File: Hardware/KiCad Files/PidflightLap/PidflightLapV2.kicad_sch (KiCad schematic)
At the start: 27 parts, among them SW1 SW_SPST, U1 HC_06, U2 RX5808, U3 Arduino_Nano_v3.x, U4 RX5808, U5 Arduino_Nano_v3.x, U6 RX5808, U7 Arduino_Nano_v3.x, U8 RX5808, U9 Arduino_Nano_v3.x

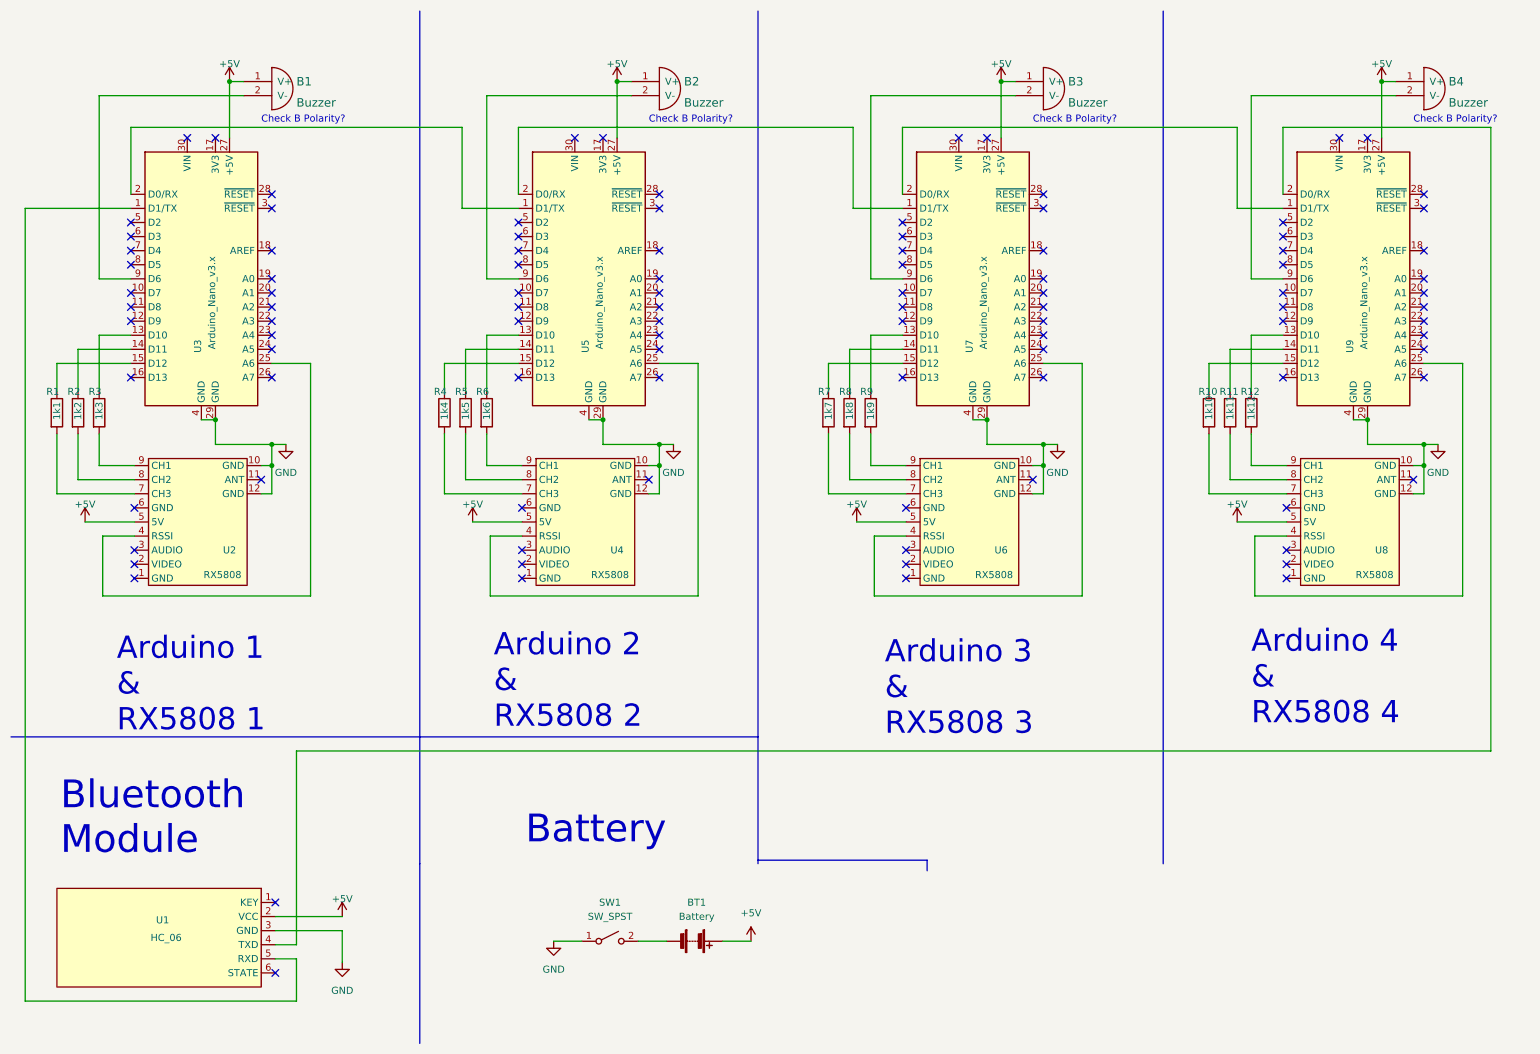
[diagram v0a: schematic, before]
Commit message: Cleaned Up Files and added Bevels and BOM
removed some pointless KiCAD files I had accidently added created as well as beveled all the 90 degree connections on the PCB file
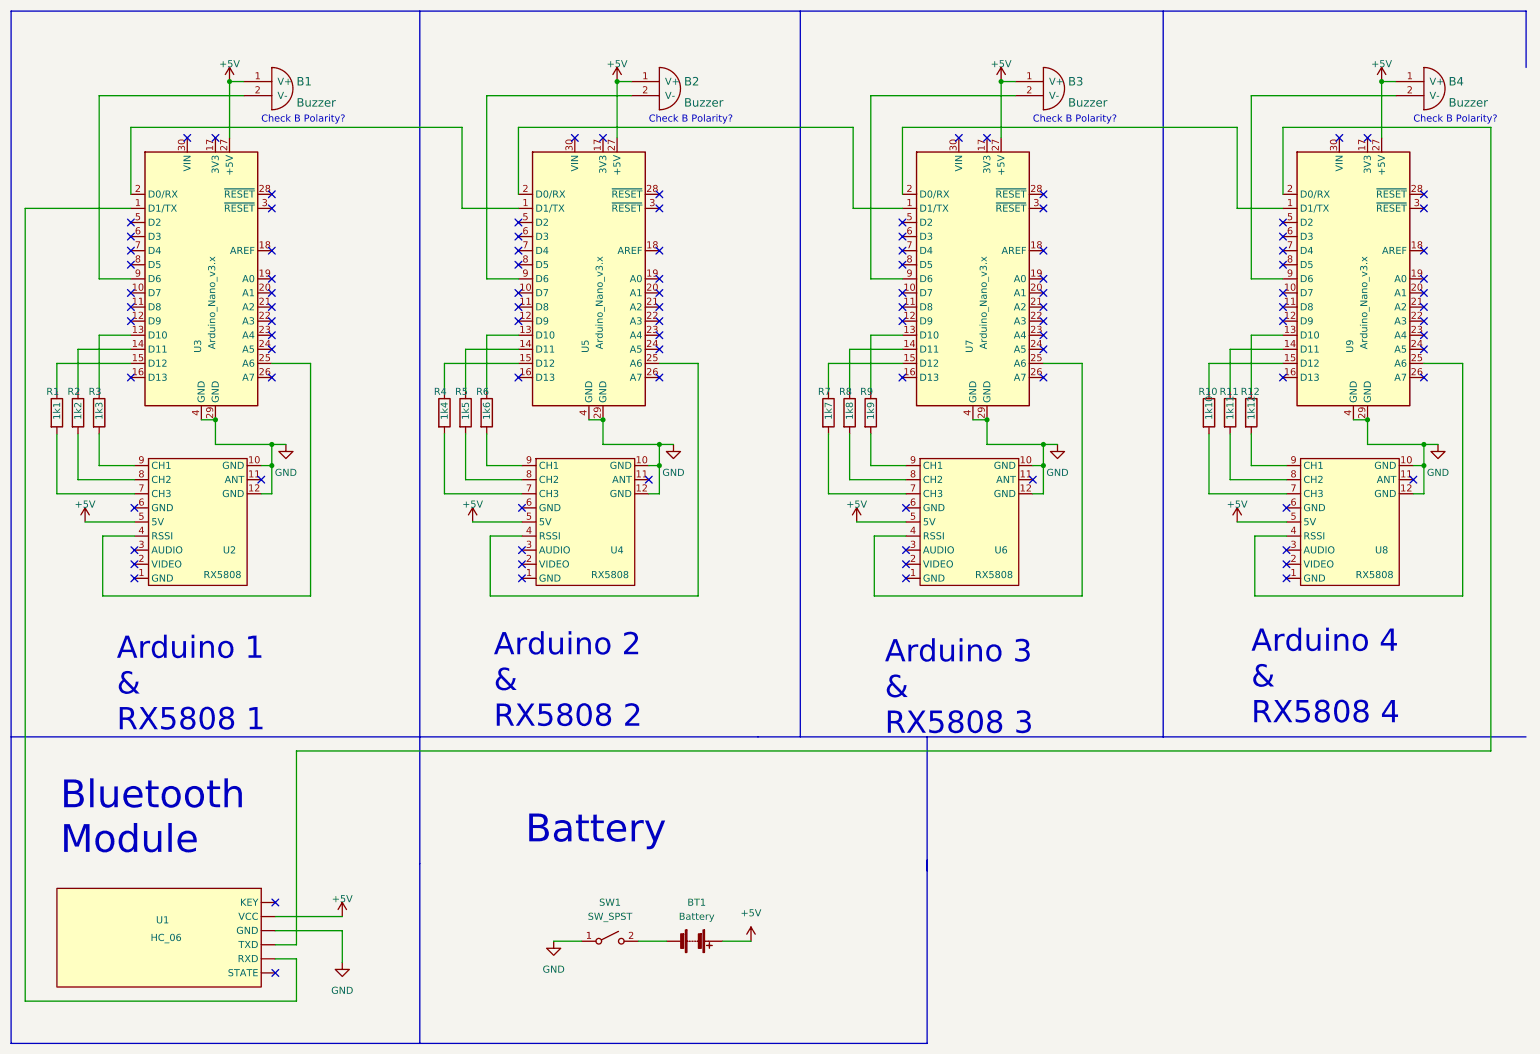
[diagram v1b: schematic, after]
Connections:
- net +5V: now also U1. (VCC); no longer U1.2 (VCC)
- net GND: now also U1. (VCC); no longer U1.3 (GND)
- net at U9.2 (D0/RX): now also U1. (VCC); no longer U1.4 (TXD)
- net at U3.1 (D1/TX): now also U1. (VCC); no longer U1.5 (RXD)
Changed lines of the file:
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@@
   (junction (at 187.96 85.725) (diameter 0) (color 0 0 0 1)
   )
+  (junction (at 128.905 90.17) (diameter 0) (color 0 0 0 1)
+  )
+  (junction (at 121.285 24.765) (diameter 0) (color 255 0 0 1)
+  )
   (junction (at 48.895 85.725) (diameter 0) (color 0 0 0 1)
-  )
-  (junction (at 128.905 90.17) (diameter 0) (color 0 0 0 1)
-  )
-  (junction (at 121.285 24.765) (diameter 0) (color 255 0 0 1)
   )
   (no_connect (at 118.745 34.925))
@@
     (stroke (width 0) (type default) (color 0 0 0 1))
   )
+  (polyline (pts (xy 12.065 12.065) (xy 285.115 12.065))
+    (stroke (width 0) (type default) (color 0 0 0 0))
+  )
   (wire (pts (xy 33.655 45.085) (xy 33.655 33.02))
     (stroke (width 0) (type default) (color 255 0 255 1))
@@
     (stroke (width 0) (type default) (color 0 0 0 1))
   )
+  (wire (pts (xy 48.895 85.725) (xy 48.895 90.17))
+    (stroke (width 0) (type default) (color 0 0 0 1))
+  )
   (wire (pts (xy 27.94 88.265) (xy 27.94 93.98))
     (stroke (width 0) (type default) (color 246 255 28 1))
@@
     (stroke (width 0) (type default) (color 0 0 0 1))
   )
+  (polyline (pts (xy 12.065 12.065) (xy 12.065 198.12))
+    (stroke (width 0) (type default) (color 0 0 0 0))
+  )
   (wire (pts (xy 63.5 190.5) (xy 63.5 182.88))
     (stroke (width 0) (type default) (color 255 0 255 1))
@@
   )
   (wire (pts (xy 59.055 99.06) (xy 57.15 99.06))
-    (stroke (width 0) (type default) (color 0 0 0 1))
-  )
-  (wire (pts (xy 48.895 85.725) (xy 48.895 90.17))
     (stroke (width 0) (type default) (color 0 0 0 1))
   )
@@
     (stroke (width 0) (type default) (color 0 0 0 1))
   )
+  (polyline (pts (xy 154.305 12.065) (xy 154.305 142.875))
+    (stroke (width 0) (type default) (color 0 0 0 0))
+  )
   (wire (pts (xy 187.96 85.725) (xy 187.96 90.17))
     (stroke (width 0) (type default) (color 0 0 0 1))
@@
     (stroke (width 0) (type default) (color 246 255 28 1))
   )
+  (polyline (pts (xy 285.115 12.065) (xy 285.115 22.225))
+    (stroke (width 0) (type default) (color 0 0 0 0))
+  )
   (wire (pts (xy 256.54 90.17) (xy 266.7 90.17))
     (stroke (width 0) (type default) (color 0 0 0 1))
@@
     (stroke (width 0) (type default) (color 0 0 0 1))
   )
+  (polyline (pts (xy 85.725 198.12) (xy 177.165 198.12))
+    (stroke (width 0) (type default) (color 0 0 0 0))
+  )
   (wire (pts (xy 93.345 33.02) (xy 93.345 47.625))
     (stroke (width 0) (type default) (color 255 0 255 1))
@@
   (wire (pts (xy 27.94 80.645) (xy 27.94 70.485))
     (stroke (width 0) (type default) (color 246 255 28 1))
+  )
+  (polyline (pts (xy 146.685 142.875) (xy 219.71 142.875))
+    (stroke (width 0) (type default) (color 0 0 0 0))
   )
   (wire (pts (xy 190.5 24.765) (xy 193.04 24.765))
@@
     (stroke (width 0) (type default) (color 0 0 0 1))
   )
-  (polyline (pts (xy 219.71 12.065) (xy 219.71 165.735))
+  (polyline (pts (xy 219.71 12.065) (xy 219.71 142.875))
     (stroke (width 0) (type default) (color 0 0 0 0))
   )
@@
     (stroke (width 0) (type default) (color 255 0 255 1))
   )
+  (polyline (pts (xy 219.71 142.875) (xy 285.115 142.875))
+    (stroke (width 0) (type default) (color 0 0 0 0))
+  )
   (polyline (pts (xy 85.725 12.065) (xy 85.725 165.735))
     (stroke (width 0) (type default) (color 0 0 0 0))
@@
     (stroke (width 0) (type default) (color 0 0 0 1))
   )
+  (wire (pts (xy 34.29 106.68) (xy 28.575 106.68))
+    (stroke (width 0) (type default) (color 0 0 0 0))
+  )
+  (wire (pts (xy 167.64 106.68) (xy 167.64 117.475))
+    (stroke (width 0) (type default) (color 0 0 0 0))
+  )
   (wire (pts (xy 46.355 85.725) (xy 48.895 85.725))
     (stroke (width 0) (type default) (color 0 0 0 1))
-  )
-  (wire (pts (xy 34.29 106.68) (xy 28.575 106.68))
-    (stroke (width 0) (type default) (color 0 0 0 0))
-  )
-  (wire (pts (xy 167.64 106.68) (xy 167.64 117.475))
-    (stroke (width 0) (type default) (color 0 0 0 0))
   )
   (wire (pts (xy 235.585 27.305) (xy 261.62 27.305))
@@
     (stroke (width 0) (type default) (color 255 0 0 1))
   )
-  (polyline (pts (xy 146.685 165.1) (xy 177.165 165.1))
-    (stroke (width 0) (type default) (color 0 0 0 0))
-  )
   (wire (pts (xy 104.14 96.52) (xy 93.98 96.52))
     (stroke (width 0) (type default) (color 15 255 0 1))
@@
     (stroke (width 0) (type default) (color 0 0 0 0))
   )
-  (polyline (pts (xy 146.685 12.065) (xy 146.685 165.735))
-    (stroke (width 0) (type default) (color 0 0 0 0))
-  )
   (wire (pts (xy 266.7 93.98) (xy 266.7 99.06))
     (stroke (width 0) (type default) (color 0 0 0 1))
@@
   (wire (pts (xy 128.905 90.17) (xy 131.445 90.17))
     (stroke (width 0) (type default) (color 0 0 0 1))
+  )
+  (polyline (pts (xy 177.165 198.12) (xy 177.165 142.875))
+    (stroke (width 0) (type default) (color 0 0 0 0))
   )
   (wire (pts (xy 167.005 70.485) (xy 172.72 70.485))
@@
   (wire (pts (xy 235.585 88.265) (xy 235.585 93.98))
     (stroke (width 0) (type default) (color 246 255 28 1))
+  )
+  (polyline (pts (xy 85.725 198.12) (xy 12.065 198.12))
+    (stroke (width 0) (type default) (color 0 0 0 0))
   )
   (wire (pts (xy 34.29 99.06) (xy 20.32 99.06))
@@
       (effects (font (size 1.27 1.27)) hide)
     )
-    (pin "1")
-    (pin "2")
-    (pin "3")
-    (pin "4")
-    (pin "5")
-    (pin "6")
+    (pin "")
+    (pin "")
+    (pin "")
+    (pin "")
+    (pin "")
+    (pin "")
   )
   (symbol (lib_id "power:+5V") (at 71.755 175.26 0) (unit 1)
